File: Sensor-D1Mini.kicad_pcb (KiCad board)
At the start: 2 copper layers, 45.1 x 89.9 mm, 13 parts, among them J1 Solar Panel, J2 Battery, SW1 Sensor Number, U1 BME280, U2 mini_esp32, U4 TP4056

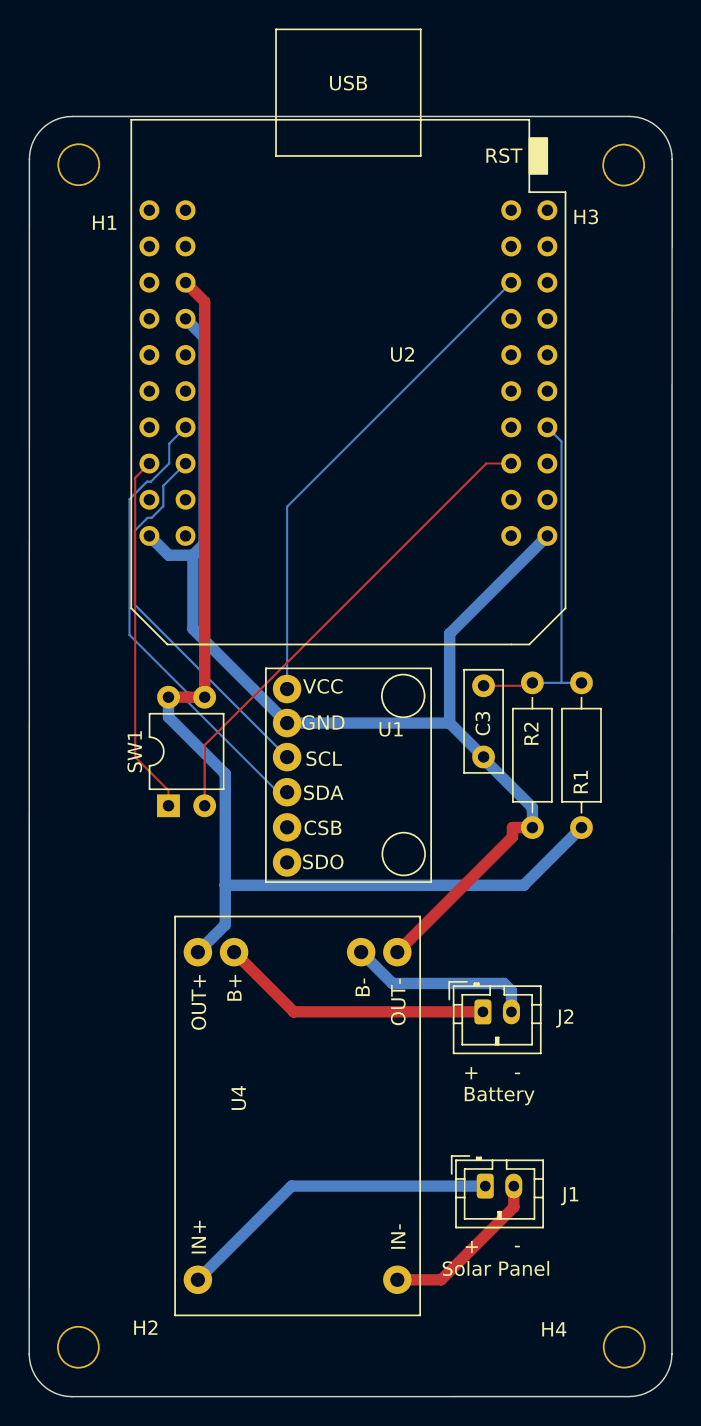
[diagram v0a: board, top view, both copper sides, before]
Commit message: 3.3V for switches
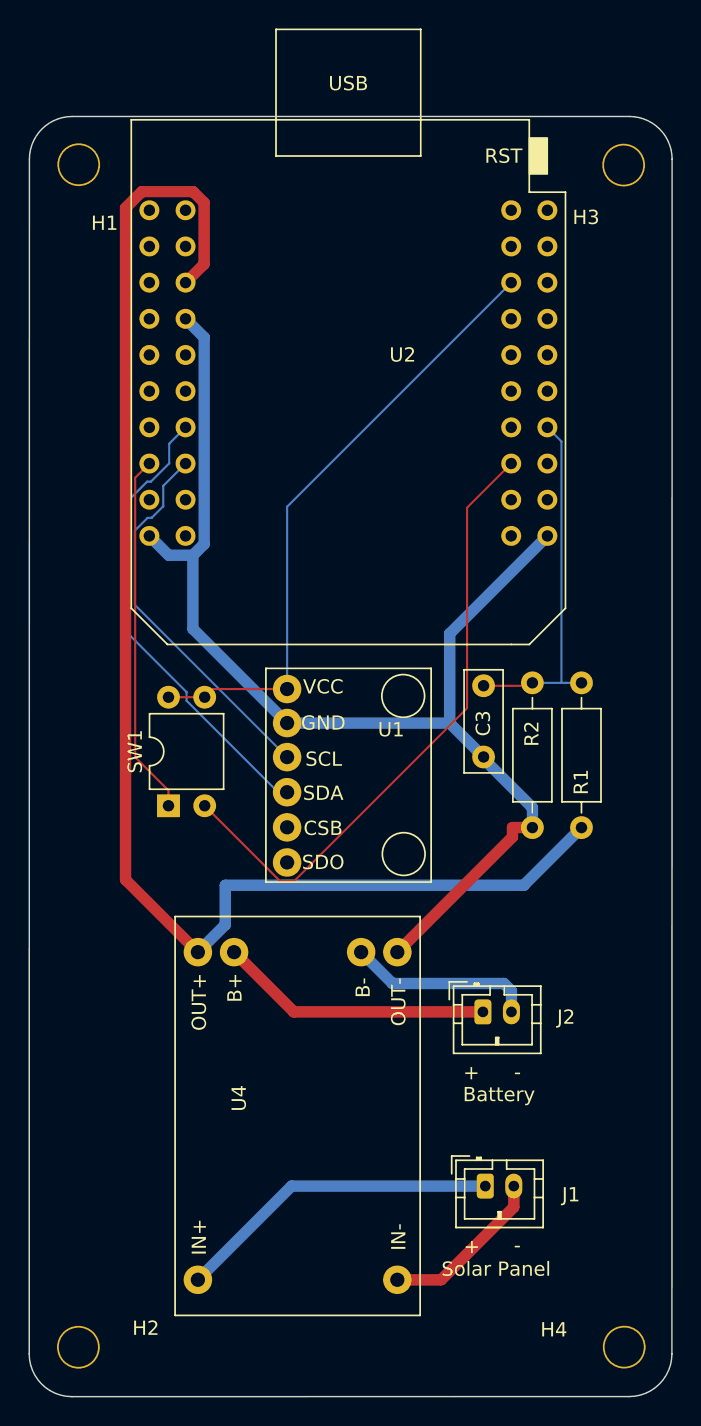
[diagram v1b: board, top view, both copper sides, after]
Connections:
- SW1 pad 3: +5V -> +3.3V
- SW1 pad 4: +5V -> +3.3V
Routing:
- net +5V: track 79.2 -> 99.0 mm
- net BIT1: track 34.0 -> 44.1 mm
- net +3.3V: track 35.0 -> 43.6 mm
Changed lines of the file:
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@@
       (net 4 "BIT1") (pintype "passive"))
     (pad "3" thru_hole oval (at 7.62 2.54 90) (size 1.6 1.6) (drill 0.8) (layers *.Cu *.Mask)
-      (net 1 "+5V") (pintype "passive"))
+      (net 27 "+3.3V") (pintype "passive"))
     (pad "4" thru_hole oval (at 7.62 0 90) (size 1.6 1.6) (drill 0.8) (layers *.Cu *.Mask)
-      (net 1 "+5V") (pintype "passive"))
+      (net 27 "+3.3V") (pintype "passive"))
     (model "${KICAD6_3DMODEL_DIR}/Package_DIP.3dshapes/DIP-4_W7.62mm.wrl"
       (offset (xyz 0 0 0))
@@
     (effects (font (size 1 1) (thickness 0.25)))
   )
-  (segment (start 88.1004 101.5839) (end 89.5007 101.5839) (width 0.8) (layer "F.Cu") (net 1))
-  (segment (start 89.5007 101.5839) (end 90.6404 101.5839) (width 0.8) (layer "F.Cu") (net 1))
-  (segment (start 90.6404 73.8232) (end 90.6404 101.5839) (width 0.8) (layer "F.Cu") (net 1))
-  (segment (start 89.2981 72.4809) (end 90.6404 73.8232) (width 0.8) (layer "F.Cu") (net 1))
+  (segment (start 86.219622 66.1009) (end 85.0867 67.233822) (width 0.8) (layer "F.Cu") (net 1))
+  (segment (start 85.0867 114.402) (end 90.1642 119.4795) (width 0.8) (layer "F.Cu") (net 1))
+  (segment (start 85.0867 67.233822) (end 85.0867 114.402) (width 0.8) (layer "F.Cu") (net 1))
+  (segment (start 90.5981 71.1809) (end 90.5981 66.862422) (width 0.8) (layer "F.Cu") (net 1))
+  (segment (start 89.836578 66.1009) (end 86.219622 66.1009) (width 0.8) (layer "F.Cu") (net 1))
+  (segment (start 89.2981 72.4809) (end 90.5981 71.1809) (width 0.8) (layer "F.Cu") (net 1))
+  (segment (start 90.5981 66.862422) (end 89.836578 66.1009) (width 0.8) (layer "F.Cu") (net 1))
   (segment (start 113.0423 114.7858) (end 92.0874 114.7858) (width 0.8) (layer "B.Cu") (net 1))
-  (segment (start 88.1004 102.9842) (end 92.0874 106.9712) (width 0.8) (layer "B.Cu") (net 1))
   (segment (start 92.0874 117.5563) (end 90.1642 119.4795) (width 0.8) (layer "B.Cu") (net 1))
-  (segment (start 88.1004 101.5839) (end 88.1004 102.9842) (width 0.8) (layer "B.Cu") (net 1))
   (segment (start 117.0914 110.7367) (end 113.0423 114.7858) (width 0.8) (layer "B.Cu") (net 1))
-  (segment (start 92.0874 106.9712) (end 92.0874 114.7858) (width 0.8) (layer "B.Cu") (net 1))
   (segment (start 92.0874 114.7858) (end 92.0874 117.5563) (width 0.8) (layer "B.Cu") (net 1))
   (segment (start 112.2454 110.7351) (end 112.2454 111.3983) (width 0.8) (layer "F.Cu") (net 2))
@@
   (segment (start 85.7617 105.7899) (end 88.1004 108.1286) (width 0.15) (layer "F.Cu") (net 3))
   (segment (start 88.1004 109.2039) (end 88.1004 108.1286) (width 0.15) (layer "F.Cu") (net 3))
-  (segment (start 90.6404 104.9378) (end 90.6404 109.2039) (width 0.15) (layer "F.Cu") (net 4))
-  (segment (start 112.1581 85.1809) (end 110.3973 85.1809) (width 0.15) (layer "F.Cu") (net 4))
-  (segment (start 110.3973 85.1809) (end 90.6404 104.9378) (width 0.15) (layer "F.Cu") (net 4))
+  (segment (start 96.954416 114.458341) (end 109.05756 102.355197) (width 0.15) (layer "F.Cu") (net 4))
+  (segment (start 90.6404 109.2039) (end 95.894841 114.458341) (width 0.15) (layer "F.Cu") (net 4))
+  (segment (start 109.05756 102.355197) (end 109.05756 88.28144) (width 0.15) (layer "F.Cu") (net 4))
+  (segment (start 109.05756 88.28144) (end 112.1581 85.1809) (width 0.15) (layer "F.Cu") (net 4))
+  (segment (start 95.894841 114.458341) (end 96.954416 114.458341) (width 0.15) (layer "F.Cu") (net 4))
   (segment (start 96.7421 135.9016) (end 110.3396 135.9016) (width 0.8) (layer "B.Cu") (net 7))
   (segment (start 90.1642 142.4795) (end 96.7421 135.9016) (width 0.8) (layer "B.Cu") (net 7))
@@
   (segment (start 88.1521 85.1674) (end 86.8686 86.4509) (width 0.15) (layer "B.Cu") (net 25))
   (segment (start 89.2981 82.6409) (end 88.1521 83.7869) (width 0.15) (layer "B.Cu") (net 25))
+  (segment (start 90.6404 101.5839) (end 88.1004 101.5839) (width 0.15) (layer "F.Cu") (net 27))
+  (segment (start 91.215196 101.009104) (end 90.6404 101.5839) (width 0.15) (layer "F.Cu") (net 27))
+  (segment (start 96.426293 101.009104) (end 91.215196 101.009104) (width 0.15) (layer "F.Cu") (net 27))
   (segment (start 112.1581 72.4809) (end 96.4263 88.2127) (width 0.15) (layer "B.Cu") (net 27))
   (segment (start 96.4263 88.2127) (end 96.4263 101.0091) (width 0.15) (layer "B.Cu") (net 27))
